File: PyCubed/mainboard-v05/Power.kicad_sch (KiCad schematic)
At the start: 66 parts, among them J14 Conn_01x06, Q1 IRLML2803, Q2 MBT2222ADW1T1, Q22 NDS8434, Q3 MBT2222ADW1T1, U17 BQ25883RGER, U21 TPS7A4501DCQT, U4 ADM1176-1ARMZ-R7, U5 TPS54226PWPRPWP14_2P31X2P46-L, U6 LTC4121

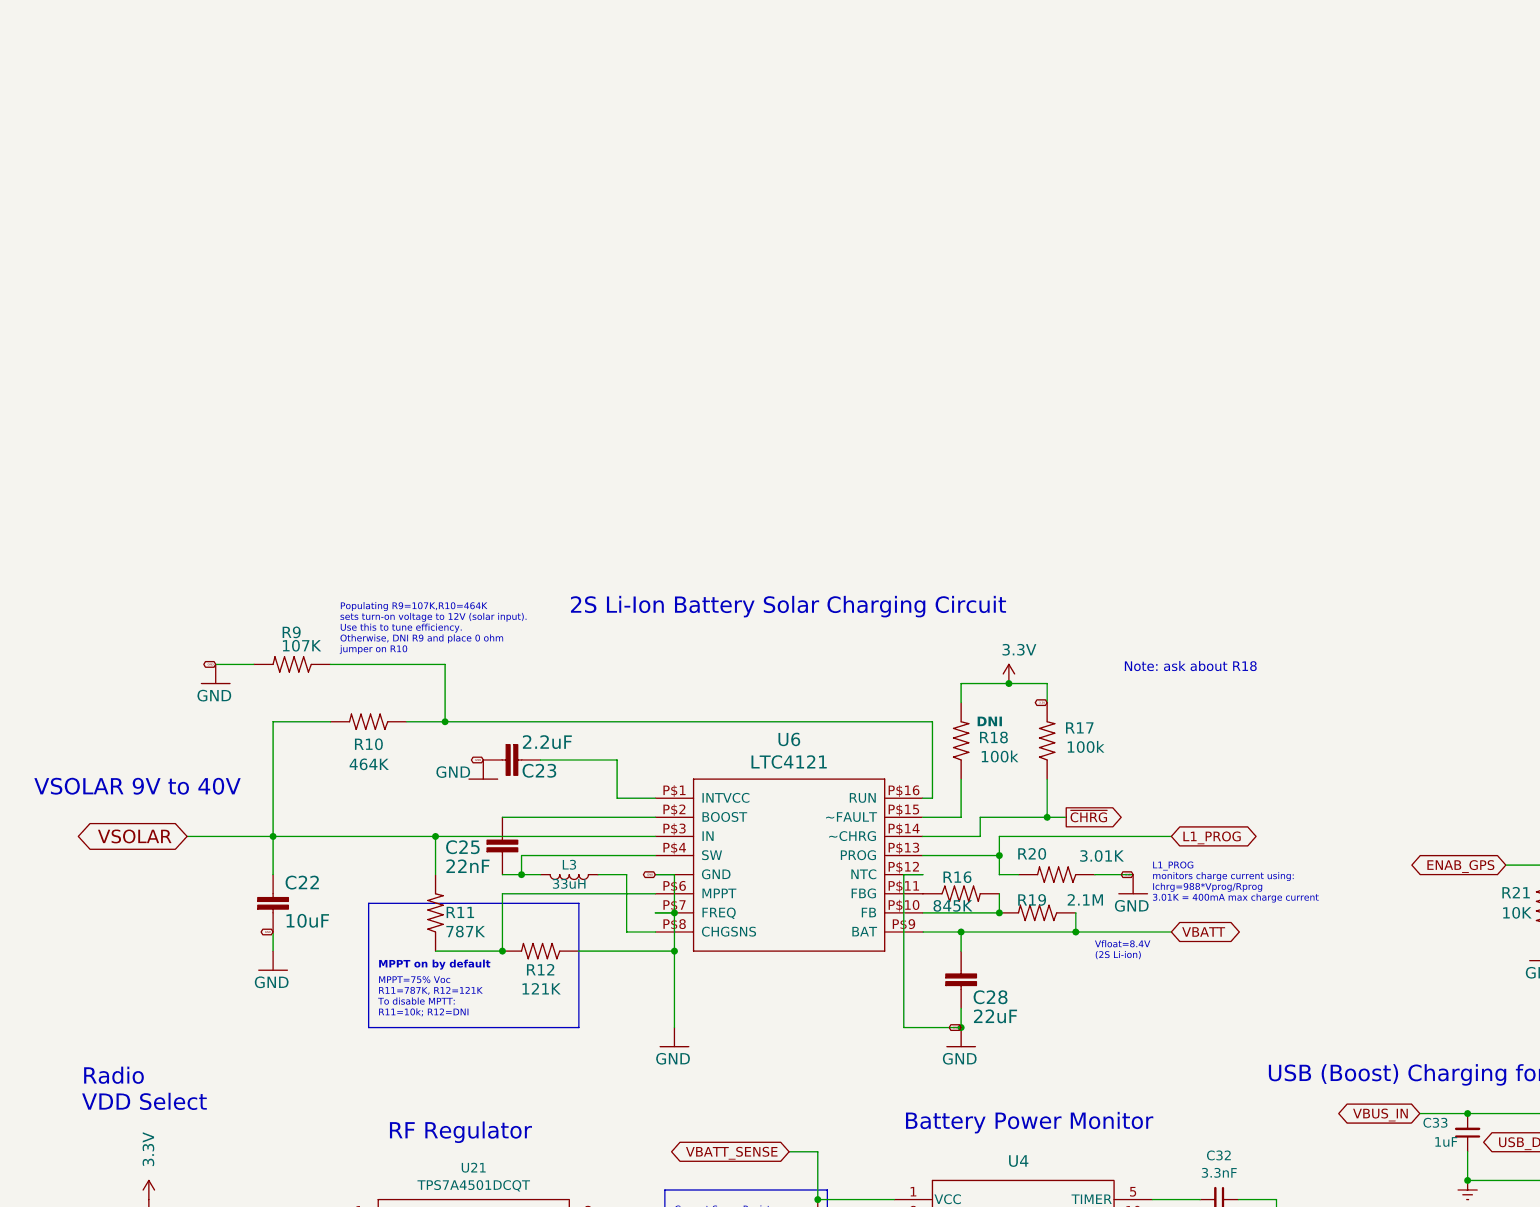
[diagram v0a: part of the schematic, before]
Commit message: added start of charging circuit
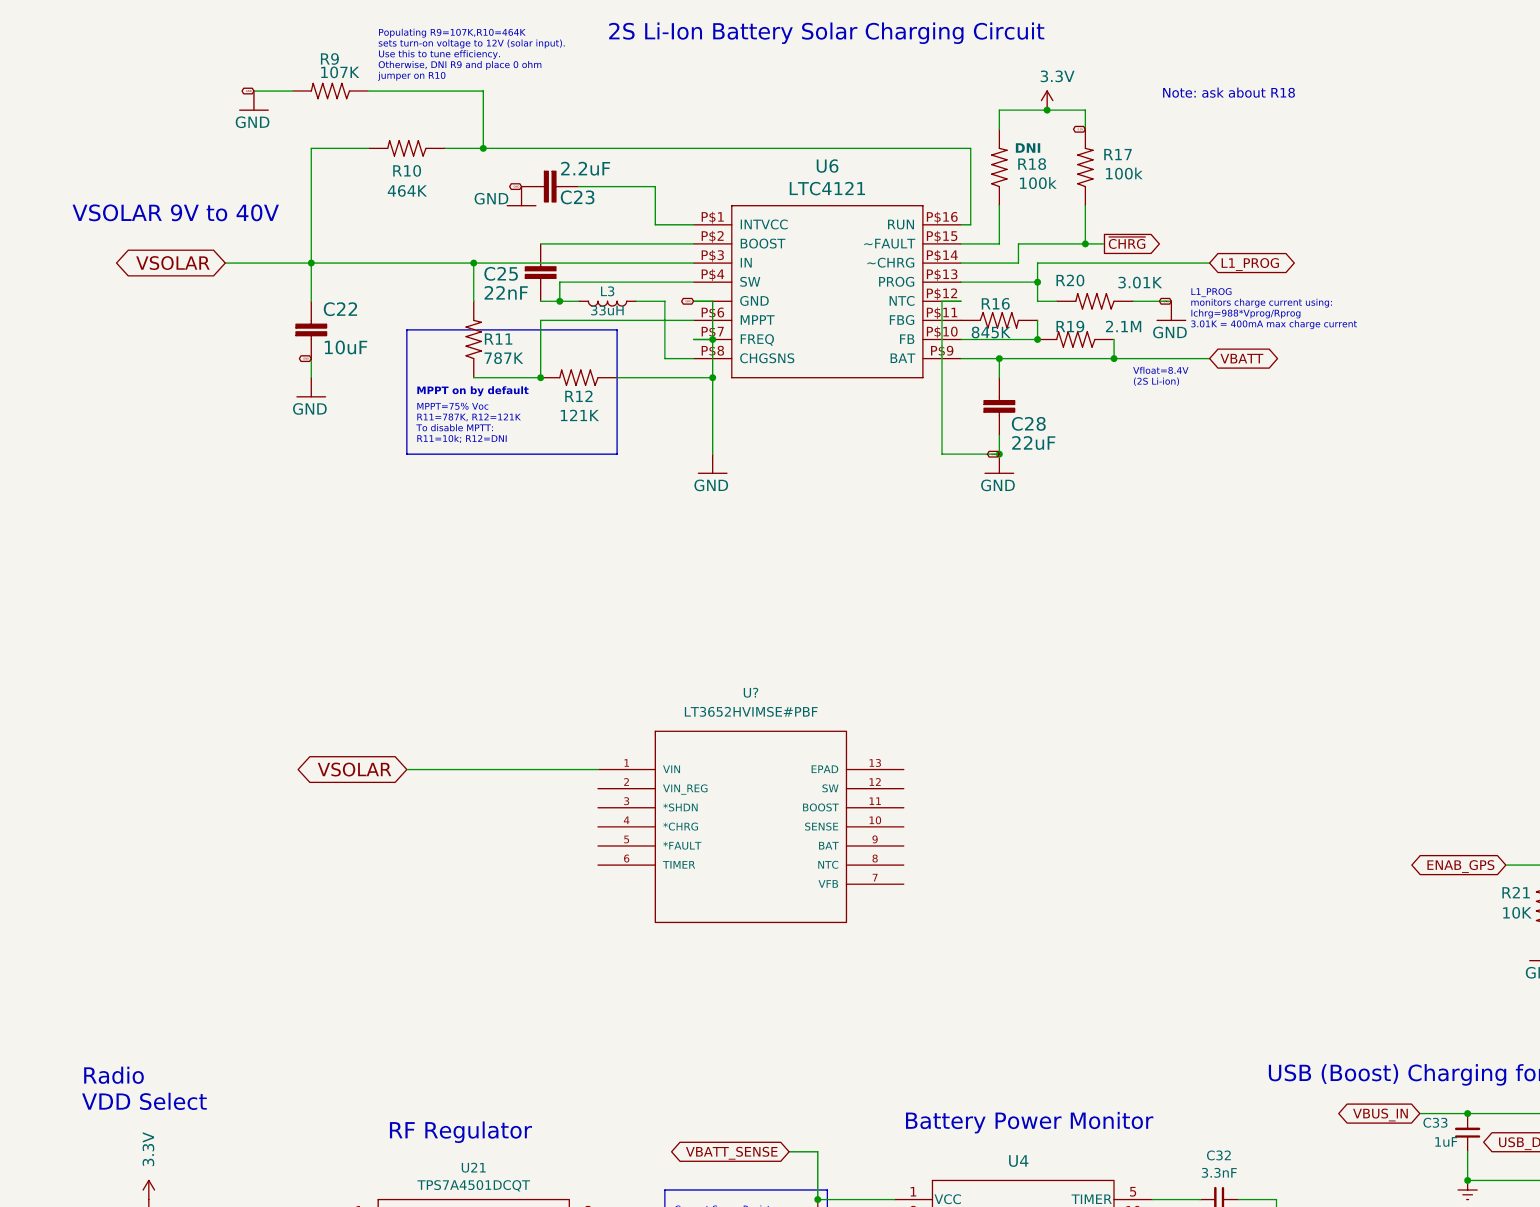
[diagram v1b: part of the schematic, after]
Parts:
- added U?: LT3652HVIMSE#PBF, MSOP-12_MSE, symbol PycubedSymbols:LT3652HVIMSE#PBF
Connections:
- net VSOLAR: now also U?.1 (VIN)
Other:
- moved on the sheet: C22, C23, C25, C28, L3, R10, R11, R12, R16, R17, R18, R19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

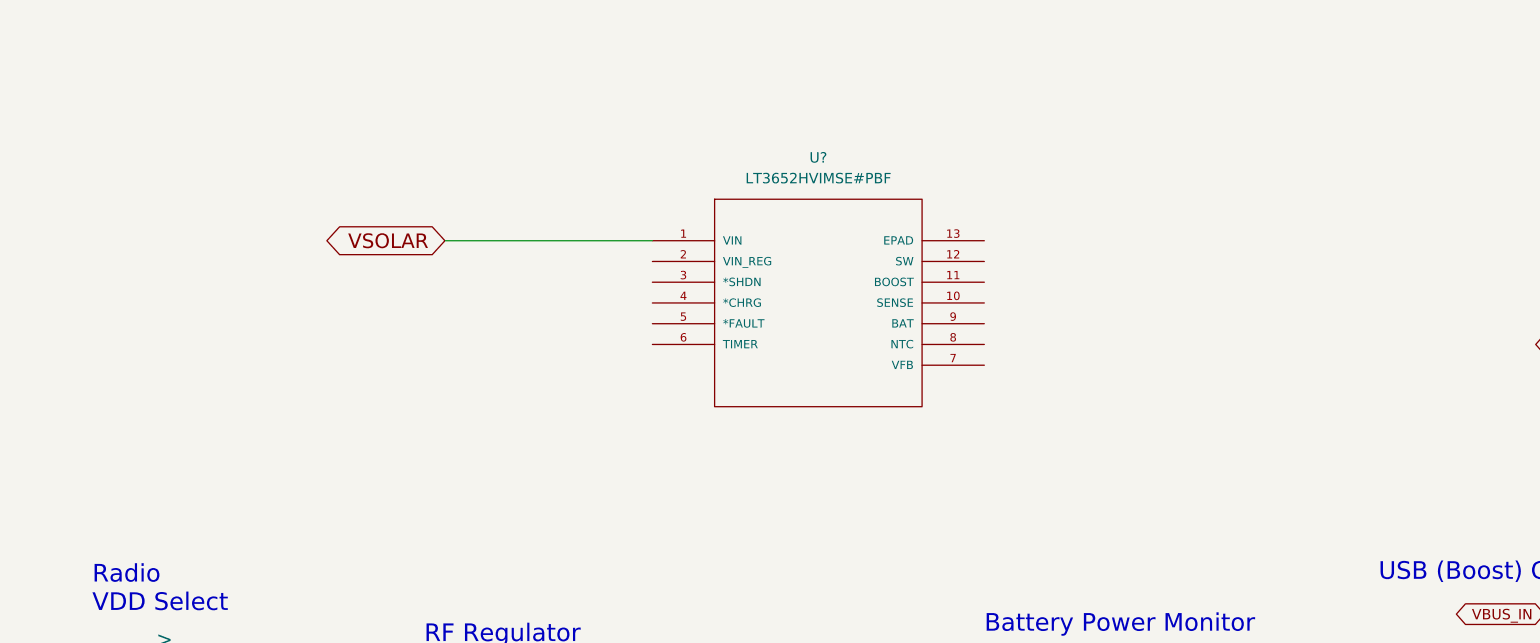
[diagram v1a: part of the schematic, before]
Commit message: added LT36HV circuit
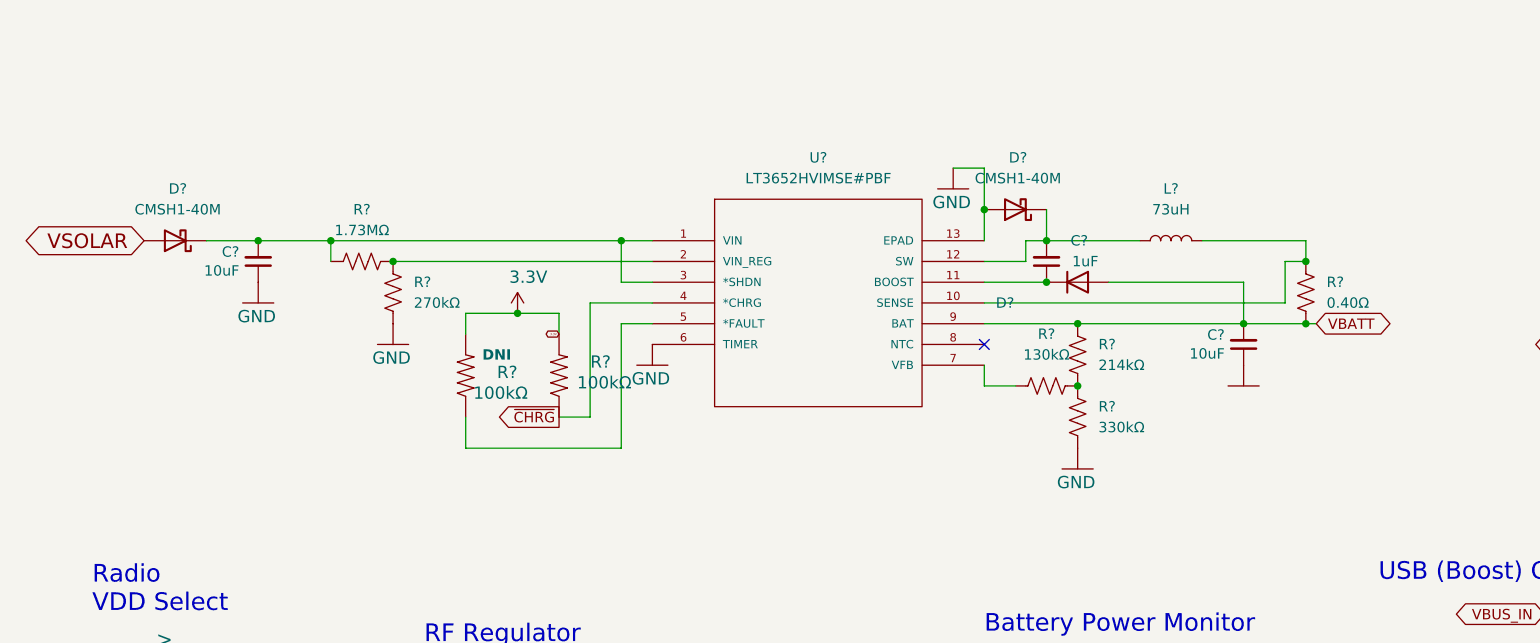
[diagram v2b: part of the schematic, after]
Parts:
- added C? (x2): 10uF, Capacitor_SMD:C_0603_1608Metric, symbol Device:C_Small
- added C?: 1uF, Capacitor_SMD:C_0603_1608Metric, symbol Device:C_Small
- added D? (x2): CMSH1-40M, symbol Device:D_Schottky
- added D?: (no value), symbol Simulation_SPICE:DIODE
- added L?: 73uH, symbol Device:L
- added R? (x2): 100kΩ, Resistor_SMD:R_0603_1608Metric, symbol mainboard:R-US_R0603
- added R?: 130kΩ, symbol Device:R_US
- added R?: 0.40Ω, symbol Device:R_US
- added R?: 1.73MΩ, symbol Device:R_US
- added R?: 214kΩ, symbol Device:R_US
- added R?: 330kΩ, symbol Device:R_US
- added R?: 270kΩ, symbol Device:R_US
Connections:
- net 3.3V: now also R?.2, R?.2
- net GND: now also U?.13 (EPAD), U?.6 (TIMER), C?.1, C?.1, D?.2 (A), R?.1, R?.2
- net VBATT: now also U?.9 (BAT), C?.2, D?.1 (A), R?.1, R?.2
- net VSOLAR: now also D?.2 (A); no longer U?.1 (VIN)
- net ~{CHRG}: now also U?.4 (*CHRG), R?.1
- net at U?.10 (SENSE): now also L?.2, R?.1
- net at U?.11 (BOOST): now also C?.1, D?.2 (K)
- net at U?.12 (SW): now also C?.2, D?.1 (K), L?.1
- net at U?.2 (VIN_REG): now also R?.2, R?.2
- net at U?.3 (*SHDN): now also U?.1 (VIN), C?.2, D?.1 (K), R?.1
- net at U?.5 (*FAULT): now also R?.1
- net at U?.7 (VFB): now also R?.1
- new net: R?.1, R?.2, R?.2
- no-connect marks 7 -> 8
